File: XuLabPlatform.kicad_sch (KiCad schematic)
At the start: 11 parts, among them J10 Servo, J11 Servo, J12 Thruster, J15 I2C, J16 UART, J4 Servo, J5 Servo, J6 Servo, J7 Servo, J8 Servo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

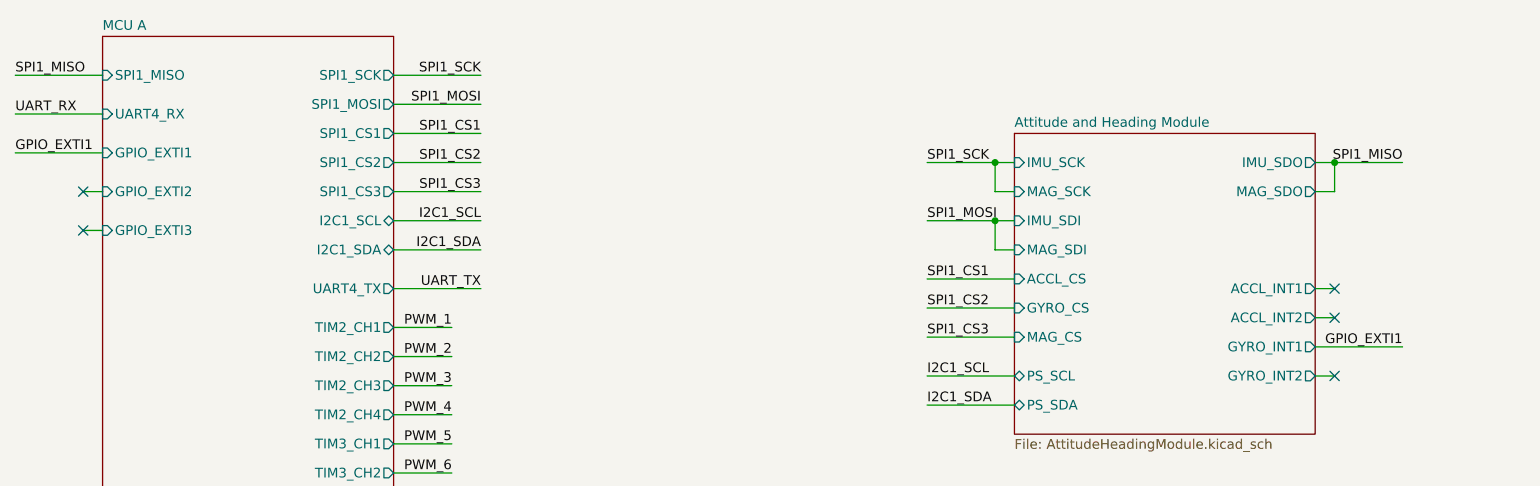
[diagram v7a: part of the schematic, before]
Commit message: Replace EXTI3 with EXTI0
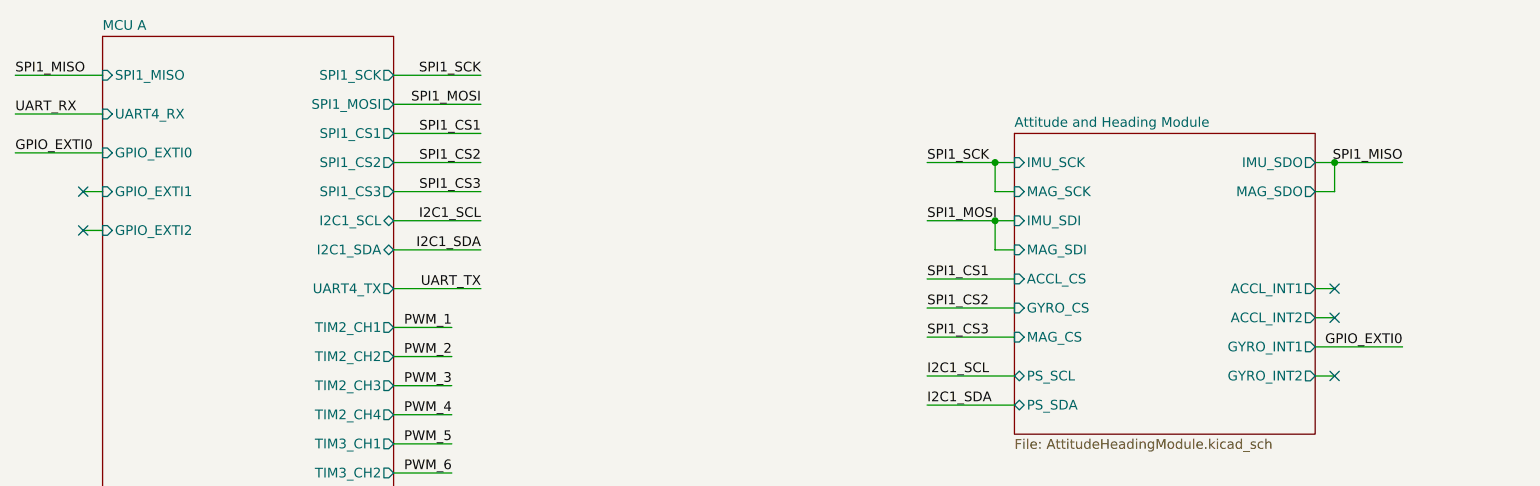
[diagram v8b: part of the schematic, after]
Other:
- sheet MCU A ports: added GPIO_EXTI0; removed GPIO_EXTI3
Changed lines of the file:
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@@
 		)
 	)
-	(label "GPIO_EXTI1"
+	(label "GPIO_EXTI0"
 		(at 39.37 58.42 0)
 		(effects
@@
 		)
 	)
-	(label "GPIO_EXTI1"
+	(label "GPIO_EXTI0"
 		(at 220.98 83.82 180)
 		(effects
@@
 			)
 		)
-		(pin "GPIO_EXTI1" input
+		(pin "GPIO_EXTI0" input
 			(at 50.8 58.42 180)
 			(effects
@@
 			)
 		)
+		(pin "GPIO_EXTI1" input
+			(at 50.8 63.5 180)
+			(effects
+				(font
+					(size 1.27 1.27)
+				)
+				(justify left)
+			)
+		)
 		(pin "GPIO_EXTI2" input
-			(at 50.8 63.5 180)
-			(effects
-				(font
-					(size 1.27 1.27)
-				)
-				(justify left)
-			)
-		)
-		(pin "GPIO_EXTI3" input
 			(at 50.8 68.58 180)
 			(effects
